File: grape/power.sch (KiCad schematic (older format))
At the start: 22 parts, among them J8 Conn_02x05_Counter_Clockwise, U6 LM4040DBZ-10, U7 R-78E3.3-0.5, U8 MIC5205-3.3YM5

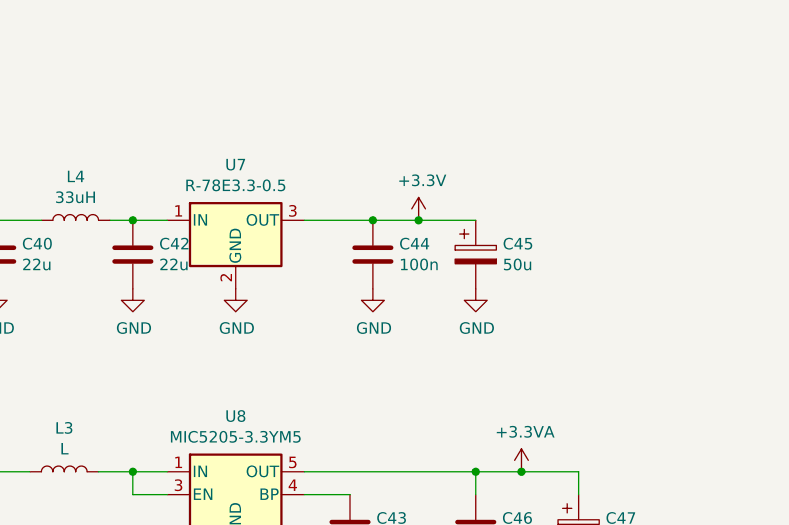
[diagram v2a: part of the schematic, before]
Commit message: Switch to TPS560430 power
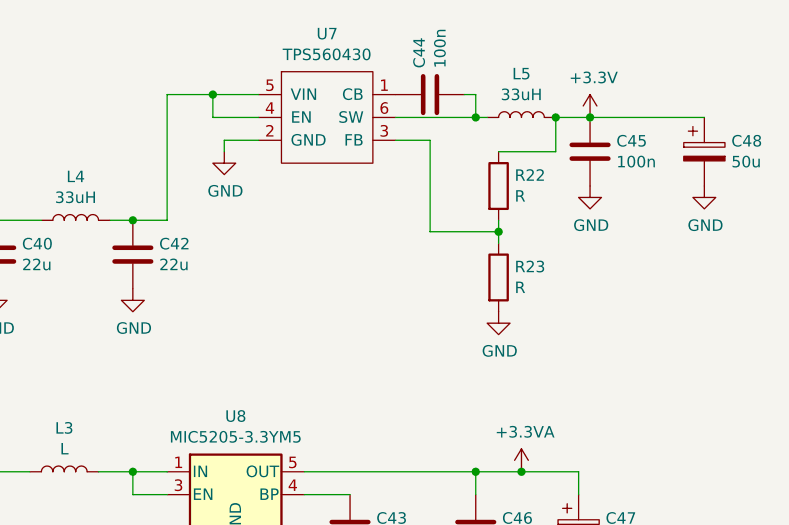
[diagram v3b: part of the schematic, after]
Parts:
- removed C45: 50u, Capacitor_Tantalum_SMD:CP_EIA-7343-31_Kemet-D_Pad2.25x2.55mm_HandSolder, symbol Device:C_Polarized
- removed U7: R-78E3.3-0.5, Converter_DCDC:Converter_DCDC_RECOM_R-78E-0.5_THT, symbol Regulator_Switching:R-78E3.3-0.5
- added C45: 100n, Capacitor_SMD:C_0805_2012Metric_Pad1.18x1.45mm_HandSolder, symbol Device:C
- added C48: 50u, Capacitor_Tantalum_SMD:CP_EIA-7343-31_Kemet-D_Pad2.25x2.55mm_HandSolder, symbol Device:C_Polarized
- added L5: 33uH, Inductor_SMD:L_Sumida_CDMC6D28_7.25x6.5mm, symbol Device:L
- added R22, R23: R, Resistor_SMD:R_0805_2012Metric_Pad1.20x1.40mm_HandSolder, symbol Device:R
- added U7: TPS560430, Package_TO_SOT_SMD:SOT-23-6_Handsoldering, symbol ursae:TPS560430
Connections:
- net +3V3: now also C45.1, C48.1, L5.2, R22.1; no longer C44.1
- net GND: now also C45.2, C48.2, R23.2, U7.2 (GND); no longer C44.2
- net at C42.1, L4.2: now also U7.4 (EN), U7.5 (VIN)
- new net: C44.1, U7.1 (CB)
- new net: R22.2, R23.1, U7.3 (FB)
- new net: C44.2, L5.1, U7.6 (SW)
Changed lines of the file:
@@
 	4700 4050 4700 4100
-$Comp
-L Regulator_Switching:R-78E3.3-0.5 U7
-U 1 1 5FC88A85
-P 7550 2200
-F 0 "U7" H 7550 2442 50  0000 C CNN
-F 1 "R-78E3.3-0.5" H 7550 2351 50  0000 C CNN
-F 2 "Converter_DCDC:Converter_DCDC_RECOM_R-78E-0.5_THT" H 7600 1950 50  0001 L CIN
-F 3 "https://www.recom-power.com/pdf/Innoline/R-78Exx-0.5.pdf" H 7550 2200 50  0001 C CNN
-	1    7550 2200
-	1    0    0    -1
-$EndComp
 $Comp
 L Device:L L4
@@
 	1    0    0    -1
 $EndComp
-$Comp
-L Device:C C44
-U 1 1 5FC8DFB5
-P 8150 2350
-F 0 "C44" H 8265 2396 50  0000 L CNN
-F 1 "100n" H 8265 2305 50  0000 L CNN
-F 2 "Capacitor_SMD:C_0805_2012Metric_Pad1.18x1.45mm_HandSolder" H 8188 2200 50  0001 C CNN
-F 3 "~" H 8150 2350 50  0001 C CNN
-	1    8150 2350
-	1    0    0    -1
-$EndComp
-$Comp
-L Device:C_Polarized C45
-U 1 1 5FC8E743
-P 8600 2350
-F 0 "C45" H 8718 2396 50  0000 L CNN
-F 1 "50u" H 8718 2305 50  0000 L CNN
-F 2 "Capacitor_Tantalum_SMD:CP_EIA-7343-31_Kemet-D_Pad2.25x2.55mm_HandSolder" H 8638 2200 50  0001 C CNN
-F 3 "~" H 8600 2350 50  0001 C CNN
-	1    8600 2350
-	1    0    0    -1
-$EndComp
 Wire Wire Line
 	6500 2200 6700 2200
@@
 	7100 2200 7250 2200
 Connection ~ 7100 2200
-Wire Wire Line
-	7850 2200 8150 2200
-Wire Wire Line
-	8150 2200 8350 2200
-Connection ~ 8150 2200
 $Comp
 L power:GND #PWR084
@@
 $EndComp
 $Comp
-L power:GND #PWR086
-U 1 1 5FC903E4
-P 7550 2500
-F 0 "#PWR086" H 7550 2250 50  0001 C CNN
-F 1 "GND" H 7555 2327 50  0000 C CNN
-F 2 "" H 7550 2500 50  0001 C CNN
-F 3 "" H 7550 2500 50  0001 C CNN
-	1    7550 2500
-	1    0    0    -1
-$EndComp
-$Comp
-L power:GND #PWR089
-U 1 1 5FC90B04
-P 8150 2500
-F 0 "#PWR089" H 8150 2250 50  0001 C CNN
-F 1 "GND" H 8155 2327 50  0000 C CNN
-F 2 "" H 8150 2500 50  0001 C CNN
-F 3 "" H 8150 2500 50  0001 C CNN
-	1    8150 2500
-	1    0    0    -1
-$EndComp
-$Comp
-L power:GND #PWR091
-U 1 1 5FC90CE5
-P 8600 2500
-F 0 "#PWR091" H 8600 2250 50  0001 C CNN
-F 1 "GND" H 8605 2327 50  0000 C CNN
-F 2 "" H 8600 2500 50  0001 C CNN
-F 3 "" H 8600 2500 50  0001 C CNN
-	1    8600 2500
-	1    0    0    -1
-$EndComp
-$Comp
 L power:+3.3V #PWR090
 U 1 1 5FC9112C
-P 8350 2200
-F 0 "#PWR090" H 8350 2050 50  0001 C CNN
-F 1 "+3.3V" H 8365 2373 50  0000 C CNN
-F 2 "" H 8350 2200 50  0001 C CNN
-F 3 "" H 8350 2200 50  0001 C CNN
-	1    8350 2200
-	1    0    0    -1
-$EndComp
-Connection ~ 8350 2200
-Wire Wire Line
-	8350 2200 8600 2200
+P 9100 1750
+F 0 "#PWR090" H 9100 1600 50  0001 C CNN
+F 1 "+3.3V" H 9115 1923 50  0000 C CNN
+F 2 "" H 9100 1750 50  0001 C CNN
+F 3 "" H 9100 1750 50  0001 C CNN
+	1    9100 1750
+	1    0    0    -1
+$EndComp
 Wire Wire Line
 	4150 3650 4150 2200
@@
 Wire Wire Line
 	8800 3300 9050 3300
+$Comp
+L ursae:TPS560430 U7
+U 1 1 5FE82595
+P 7950 1950
+F 0 "U7" H 7950 2515 50  0000 C CNN
+F 1 "TPS560430" H 7950 2424 50  0000 C CNN
+F 2 "Package_TO_SOT_SMD:SOT-23-6_Handsoldering" H 7950 1950 50  0001 C CNN
+F 3 "https://www.ti.com/lit/ds/symlink/tps560430.pdf" H 7950 1950 50  0001 C CNN
+	1    7950 1950
+	1    0    0    -1
+$EndComp
+$Comp
+L Device:L L5
+U 1 1 5FE842DE
+P 8800 1750
+F 0 "L5" V 8990 1750 50  0000 C CNN
+F 1 "33uH" V 8899 1750 50  0000 C CNN
+F 2 "Inductor_SMD:L_Sumida_CDMC6D28_7.25x6.5mm" H 8800 1750 50  0001 C CNN
+F 3 "~" H 8800 1750 50  0001 C CNN
+	1    8800 1750
+	0    -1   -1   0
+$EndComp
+$Comp
+L Device:C C44
+U 1 1 5FE8523E
+P 8400 1650
+F 0 "C44" H 8515 1696 50  0000 L CNN
+F 1 "100n" H 8515 1605 50  0000 L CNN
+F 2 "Capacitor_SMD:C_0805_2012Metric_Pad1.18x1.45mm_HandSolder" H 8438 1500 50  0001 C CNN
+F 3 "~" H 8400 1650 50  0001 C CNN
+	1    8400 1650
+	0    -1   -1   0
+$EndComp
+Wire Wire Line
+	8250 1750 8600 1750
+Wire Wire Line
+	8550 1650 8600 1650
+Wire Wire Line
+	8600 1650 8600 1750
+Connection ~ 8600 1750
+Wire Wire Line
+	8600 1750 8650 1750
+Wire Wire Line
+	7650 1650 7450 1650
+Wire Wire Line
+	7450 1650 7450 1750
+Wire Wire Line
+	7450 1750 7650 1750
+$Comp
+L power:GND #PWR086
+U 1 1 5FE886D8
+P 7500 1900
+F 0 "#PWR086" H 7500 1650 50  0001 C CNN
+F 1 "GND" H 7505 1727 50  0000 C CNN
+F 2 "" H 7500 1900 50  0001 C CNN
+F 3 "" H 7500 1900 50  0001 C CNN
+	1    7500 1900
+	1    0    0    -1
+$EndComp
+Wire Wire Line
+	7650 1850 7500 1850
+Wire Wire Line
+	7500 1850 7500 1900
+$Comp
+L Device:C C45
+U 1 1 5FE899D8
+P 9100 1900
+F 0 "C45" H 9215 1946 50  0000 L CNN
+F 1 "100n" H 9215 1855 50  0000 L CNN
+F 2 "Capacitor_SMD:C_0805_2012Metric_Pad1.18x1.45mm_HandSolder" H 9138 1750 50  0001 C CNN
+F 3 "~" H 9100 1900 50  0001 C CNN
+	1    9100 1900
+	1    0    0    -1
+$EndComp
+Wire Wire Line
+	8950 1750 9100 1750
+$Comp
+L Device:R R22
+U 1 1 5FE8AD4C
+P 8700 2050
+F 0 "R22" H 8770 2096 50  0000 L CNN
+F 1 "R" H 8770 2005 50  0000 L CNN
+F 2 "Resistor_SMD:R_0805_2012Metric_Pad1.20x1.40mm_HandSolder" V 8630 2050 50  0001 C CNN
+F 3 "~" H 8700 2050 50  0001 C CNN
+	1    8700 2050
+	1    0    0    -1
+$EndComp
+$Comp
+L Device:R R23
+U 1 1 5FE8B13B
+P 8700 2450
+F 0 "R23" H 8770 2496 50  0000 L CNN
+F 1 "R" H 8770 2405 50  0000 L CNN
+F 2 "Resistor_SMD:R_0805_2012Metric_Pad1.20x1.40mm_HandSolder" V 8630 2450 50  0001 C CNN
+F 3 "~" H 8700 2450 50  0001 C CNN
+	1    8700 2450
+	1    0    0    -1
+$EndComp
+Wire Wire Line
+	8250 1850 8400 1850
+Wire Wire Line
+	8400 1850 8400 2250
+Wire Wire Line
+	8400 2250 8700 2250
+Wire Wire Line
+	8700 2250 8700 2200
+Wire Wire Line
+	8700 2250 8700 2300
+Connection ~ 8700 2250
+Wire Wire Line
+	8700 1900 8950 1900
+Wire Wire Line
+	8950 1900 8950 1750
+Connection ~ 8950 1750
+$Comp
+L power:GND #PWR089
+U 1 1 5FE8E123
+P 8700 2600
+F 0 "#PWR089" H 8700 2350 50  0001 C CNN
+F 1 "GND" H 8705 2427 50  0000 C CNN
+F 2 "" H 8700 2600 50  0001 C CNN
+F 3 "" H 8700 2600 50  0001 C CNN
+	1    8700 2600
+	1    0    0    -1
+$EndComp
+$Comp
+L power:GND #PWR091
+U 1 1 5FE8E51C
+P 9100 2050
+F 0 "#PWR091" H 9100 1800 50  0001 C CNN
+F 1 "GND" H 9105 1877 50  0000 C CNN
+F 2 "" H 9100 2050 50  0001 C CNN
+F 3 "" H 9100 2050 50  0001 C CNN
+	1    9100 2050
+	1    0    0    -1
+$EndComp
+Connection ~ 9100 1750
+$Comp
+L Device:C_Polarized C48
+U 1 1 5FE92D68
+P 9600 1900
+F 0 "C48" H 9718 1946 50  0000 L CNN
+F 1 "50u" H 9718 1855 50  0000 L CNN
+F 2 "Capacitor_Tantalum_SMD:CP_EIA-7343-31_Kemet-D_Pad2.25x2.55mm_HandSolder" H 9638 1750 50  0001 C CNN
+F 3 "~" H 9600 1900 50  0001 C CNN
+	1    9600 1900
+	1    0    0    -1
+$EndComp
+Wire Wire Line
+	9100 1750 9600 1750
+$Comp
+L power:GND #PWR095
+U 1 1 5FE9448C
+P 9600 2050
+F 0 "#PWR095" H 9600 1800 50  0001 C CNN
+F 1 "GND" H 9605 1877 50  0000 C CNN
+F 2 "" H 9600 2050 50  0001 C CNN
+F 3 "" H 9600 2050 50  0001 C CNN
+	1    9600 2050
+	1    0    0    -1
+$EndComp
+Wire Wire Line
+	7250 2200 7250 1650
+Wire Wire Line
+	7250 1650 7450 1650
+Connection ~ 7450 1650
 $EndSCHEMATC
